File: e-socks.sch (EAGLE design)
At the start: 93 parts, among them IC1 CC2540, IC2 741G240DCK, Q1 FA-20H(32MHz), Q2 ABS06, U2 MAX21000, X4 1296-T10

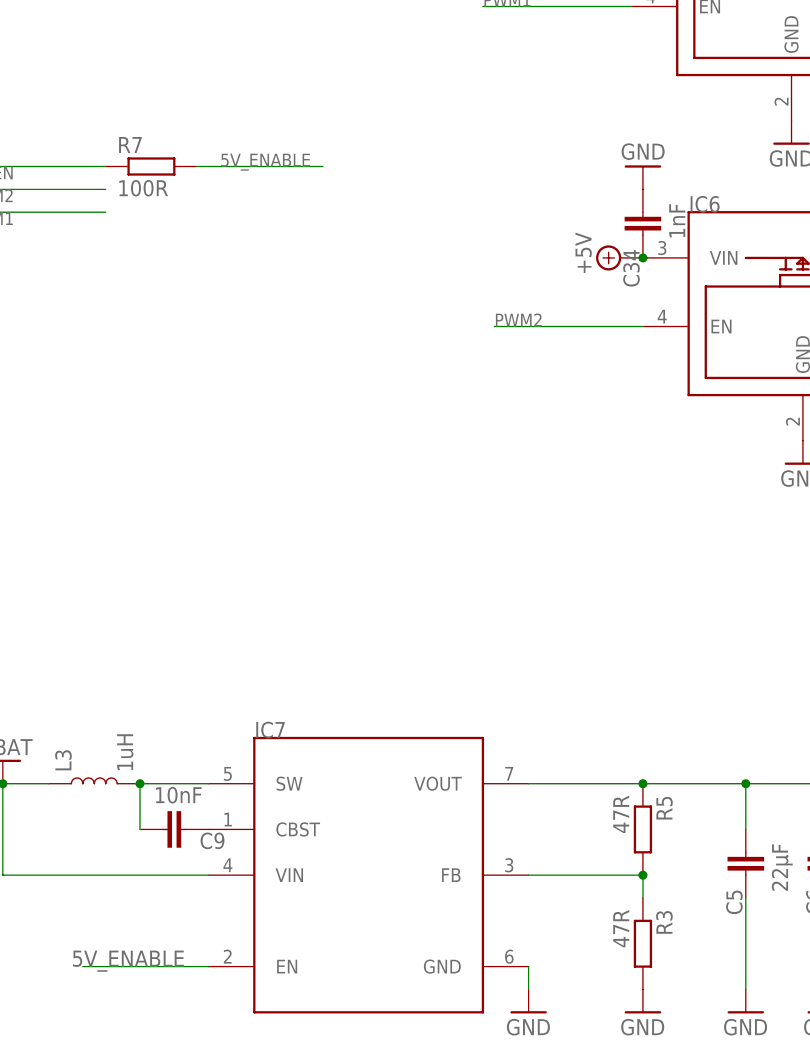
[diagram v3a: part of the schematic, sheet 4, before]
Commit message: 4K Pulldown Widerstand hinzugefügt, um den Pullup Widerstand im Reset zu überstimmen (nur für 5V-Enable), einige Widerstandswerte angepasst)
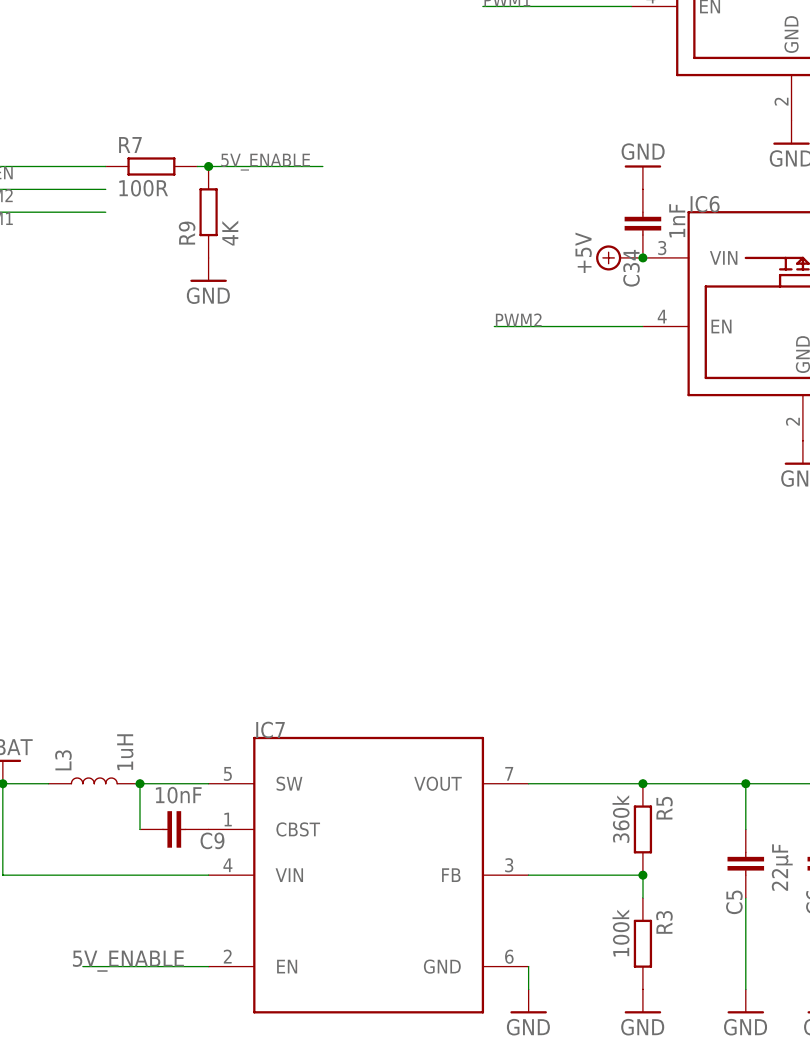
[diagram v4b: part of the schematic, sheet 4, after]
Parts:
- added R9: 4K, rcl:R-EU_R0402
- C11: value 100nF -> 220nF
- R16: value 10K -> 24K
- R19: value 4K7 -> 1K2
- R20: value 4K7k -> 1k
- R3: value 47R -> 100k
- R5: value 47R -> 360k
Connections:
- net 5V_ENABLE: now also R9.2
- net GND: now also R9.1
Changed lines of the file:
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@@
 <part name="R21" library="rcl" deviceset="R-EU_" device="R0402" value="150K"/>
 <part name="R22" library="rcl" deviceset="R-EU_" device="R0402" value="430K"/>
-<part name="C11" library="rcl" deviceset="C-EU" device="C0402" value="100nF"/>
-<part name="R20" library="rcl" deviceset="R-EU_" device="R0402" value="4K7k"/>
+<part name="C11" library="rcl" deviceset="C-EU" device="C0402" value="220nF"/>
+<part name="R20" library="rcl" deviceset="R-EU_" device="R0402" value="1k"/>
 <part name="SUPPLY7" library="supply2" deviceset="GND" device=""/>
 <part name="SUPPLY29" library="supply2" deviceset="GND" device=""/>
-<part name="R19" library="rcl" deviceset="R-EU_" device="R0402" value="4K7"/>
+<part name="R19" library="rcl" deviceset="R-EU_" device="R0402" value="1K2"/>
 <part name="SUPPLY30" library="supply2" deviceset="GND" device=""/>
 <part name="C20" library="resistor" deviceset="C-EU" device="C0402" value="2,2µF"/>
@@
 <part name="R15" library="rcl" deviceset="R-EU_" device="R0402" value="47R"/>
 <part name="GND45" library="supply1" deviceset="GND" device=""/>
-<part name="R16" library="rcl" deviceset="R-EU_" device="R0402" value="10K"/>
+<part name="R16" library="rcl" deviceset="R-EU_" device="R0402" value="24K"/>
 <part name="R17" library="rcl" deviceset="R-EU_" device="R0402" value="10K"/>
 <part name="C36" library="rcl" deviceset="C-EU" device="C0402" value="12pF"/>
@@
 <part name="U$3" library="microusb1" deviceset="MICRO-USB" device=""/>
 <part name="SUPPLY2" library="supply2" deviceset="GND" device=""/>
-<part name="R3" library="rcl" deviceset="R-EU_" device="R0402" value="47R"/>
+<part name="R3" library="rcl" deviceset="R-EU_" device="R0402" value="100k"/>
 <part name="C2" library="rcl" deviceset="C-EU" device="C0603" value="10µF"/>
 <part name="GND25" library="supply1" deviceset="GND" device=""/>
@@
 <part name="GND31" library="supply1" deviceset="GND" device=""/>
 <part name="GND32" library="supply1" deviceset="GND" device=""/>
-<part name="R5" library="rcl" deviceset="R-EU_" device="R0402" value="47R"/>
+<part name="R5" library="rcl" deviceset="R-EU_" device="R0402" value="360k"/>
 <part name="V13" library="supply0" deviceset="VBAT" device=""/>
 <part name="SUPPLY3" library="supply2" deviceset="+5V" device=""/>
@@
 <part name="GND62" library="supply1" deviceset="GND" device=""/>
 <part name="GND63" library="supply1" deviceset="GND" device=""/>
+<part name="R9" library="rcl" deviceset="R-EU_" device="R0402" value="4K"/>
+<part name="GND64" library="supply1" deviceset="GND" device=""/>
 </parts>
 <sheets>
@@
 <instance part="R8" gate="G$1" x="154.94" y="144.78" rot="R270"/>
 <instance part="LED4" gate="G$1" x="154.94" y="135.89"/>
+<instance part="R9" gate="G$1" x="68.58" y="119.38" rot="R90"/>
+<instance part="GND64" gate="1" x="68.58" y="111.76"/>
 </instances>
 <busses>
@@
 <pinref part="LED4" gate="G$1" pin="C"/>
 <wire x1="154.94" y1="130.81" x2="154.94" y2="129.54" width="0.1524" layer="91"/>
+</segment>
+<segment>
+<pinref part="R9" gate="G$1" pin="1"/>
+<pinref part="GND64" gate="1" pin="GND"/>
 </segment>
 </net>
@@
 </segment>
 <segment>
-<wire x1="81.28" y1="124.46" x2="67.31" y2="124.46" width="0.1524" layer="91"/>
+<wire x1="81.28" y1="124.46" x2="68.58" y2="124.46" width="0.1524" layer="91"/>
 <pinref part="R7" gate="G$1" pin="2"/>
 <label x="69.85" y="124.46" size="1.4224" layer="95"/>
-</segment>
-</net>
+<pinref part="R9" gate="G$1" pin="2"/>
+<wire x1="68.58" y1="124.46" x2="67.31" y2="124.46" width="0.1524" layer="91"/>
+<junction x="68.58" y="124.46"/>
+</segment>
+</net>
